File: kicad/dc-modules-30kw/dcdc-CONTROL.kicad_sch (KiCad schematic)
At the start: 35 parts

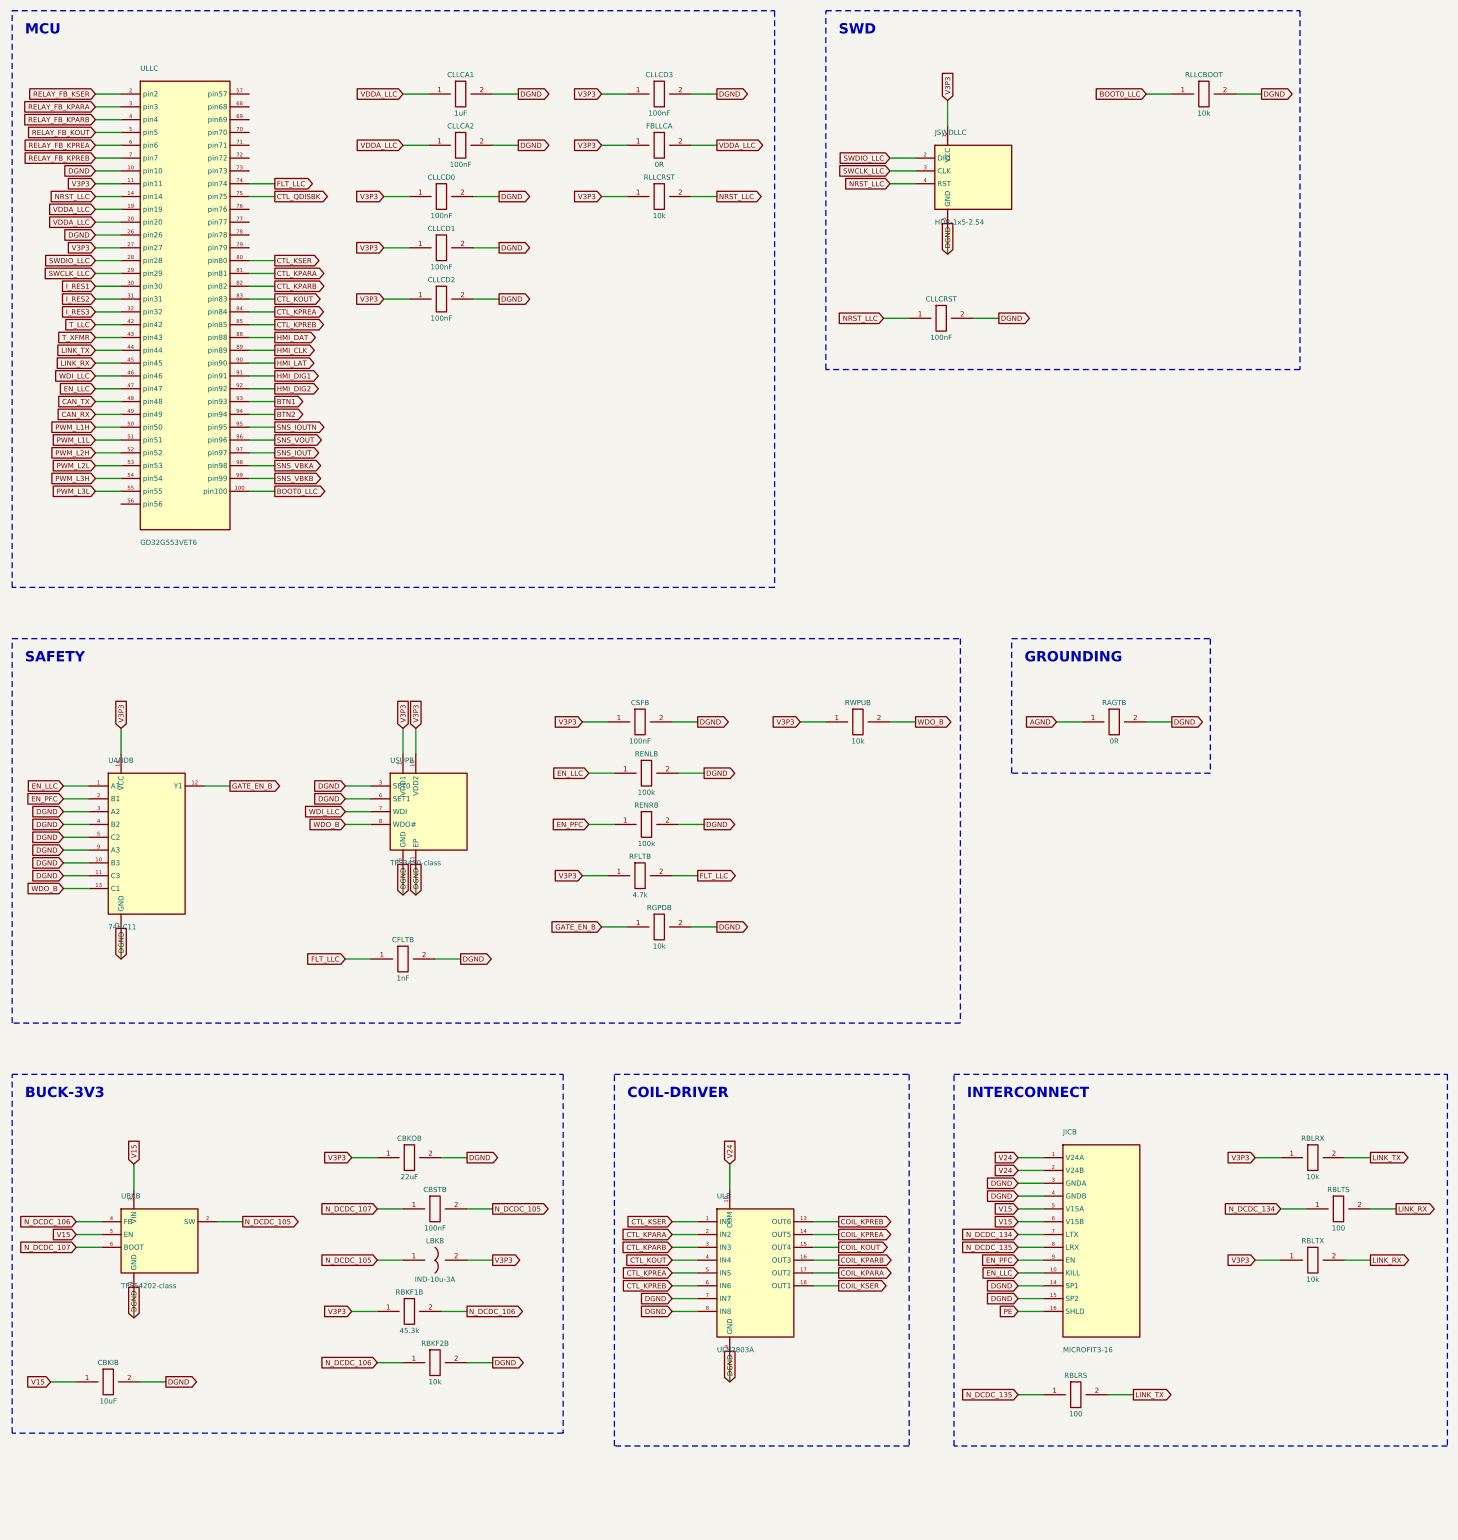
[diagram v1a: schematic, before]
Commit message: Rebuild the GD32G553VET6 pin map against the datasheet
The map was STM32G474-derived and headed pin(symbolic); gate item A6 had
recorded the GD32G553 check as pending and it was never closed. It put the
fault output on pin 74 (VSS) and BOOT0 on pin 100 (VDD) -- two hard shorts
-- and SWD on PA6/PA7, so the part was also unprogrammable as drawn.

Allocated against GD32G553xx Rev 2.0 Table 2-4 for the 120 kW worst case
(59 PFC / 80 LLC signals on 100 pins), then adversarially audited. The audit
caught a safety-critical error in the first LLC pass: PA6 cannot be
TIMER0_BRKIN0 and TIMER7_BRKIN0 at once (AF6 vs AF4, one AFSEL per pin),
which would have left four legs -- eight switches at 120 kW -- with no
hardware fault shutdown. FLT_LLC now lands on three pins, one per advanced
timer. VBAT is tied to V3P3 only; grounding it would unpower the backup
domain and kill PC13, which now carries one of those break inputs.

Applied through the remap, so the emitted netlists carry real package pins:
BOOT0 95, SWDIO 76, SWCLK 77, VDDA 37, VSSA 35, VREFP 36, all five VDD/VSS
pairs populated. Both verifiers still 100.00% (1735/1735 pins, 608
components); all review checks pass.

Four architecture decisions are documented as open rather than defaulted:
HRTIMER-vs-advanced-timer for the LLC (HRTIMER has 16 outputs, the LLC needs
24), the PFC ADC interleave scheme, LLC fan channels, and IOUT differential
mode. The map is correct and can no longer short a rail, but is not frozen.

Co-Authored-By: Claude Fable 5 <noreply@anthropic.com>
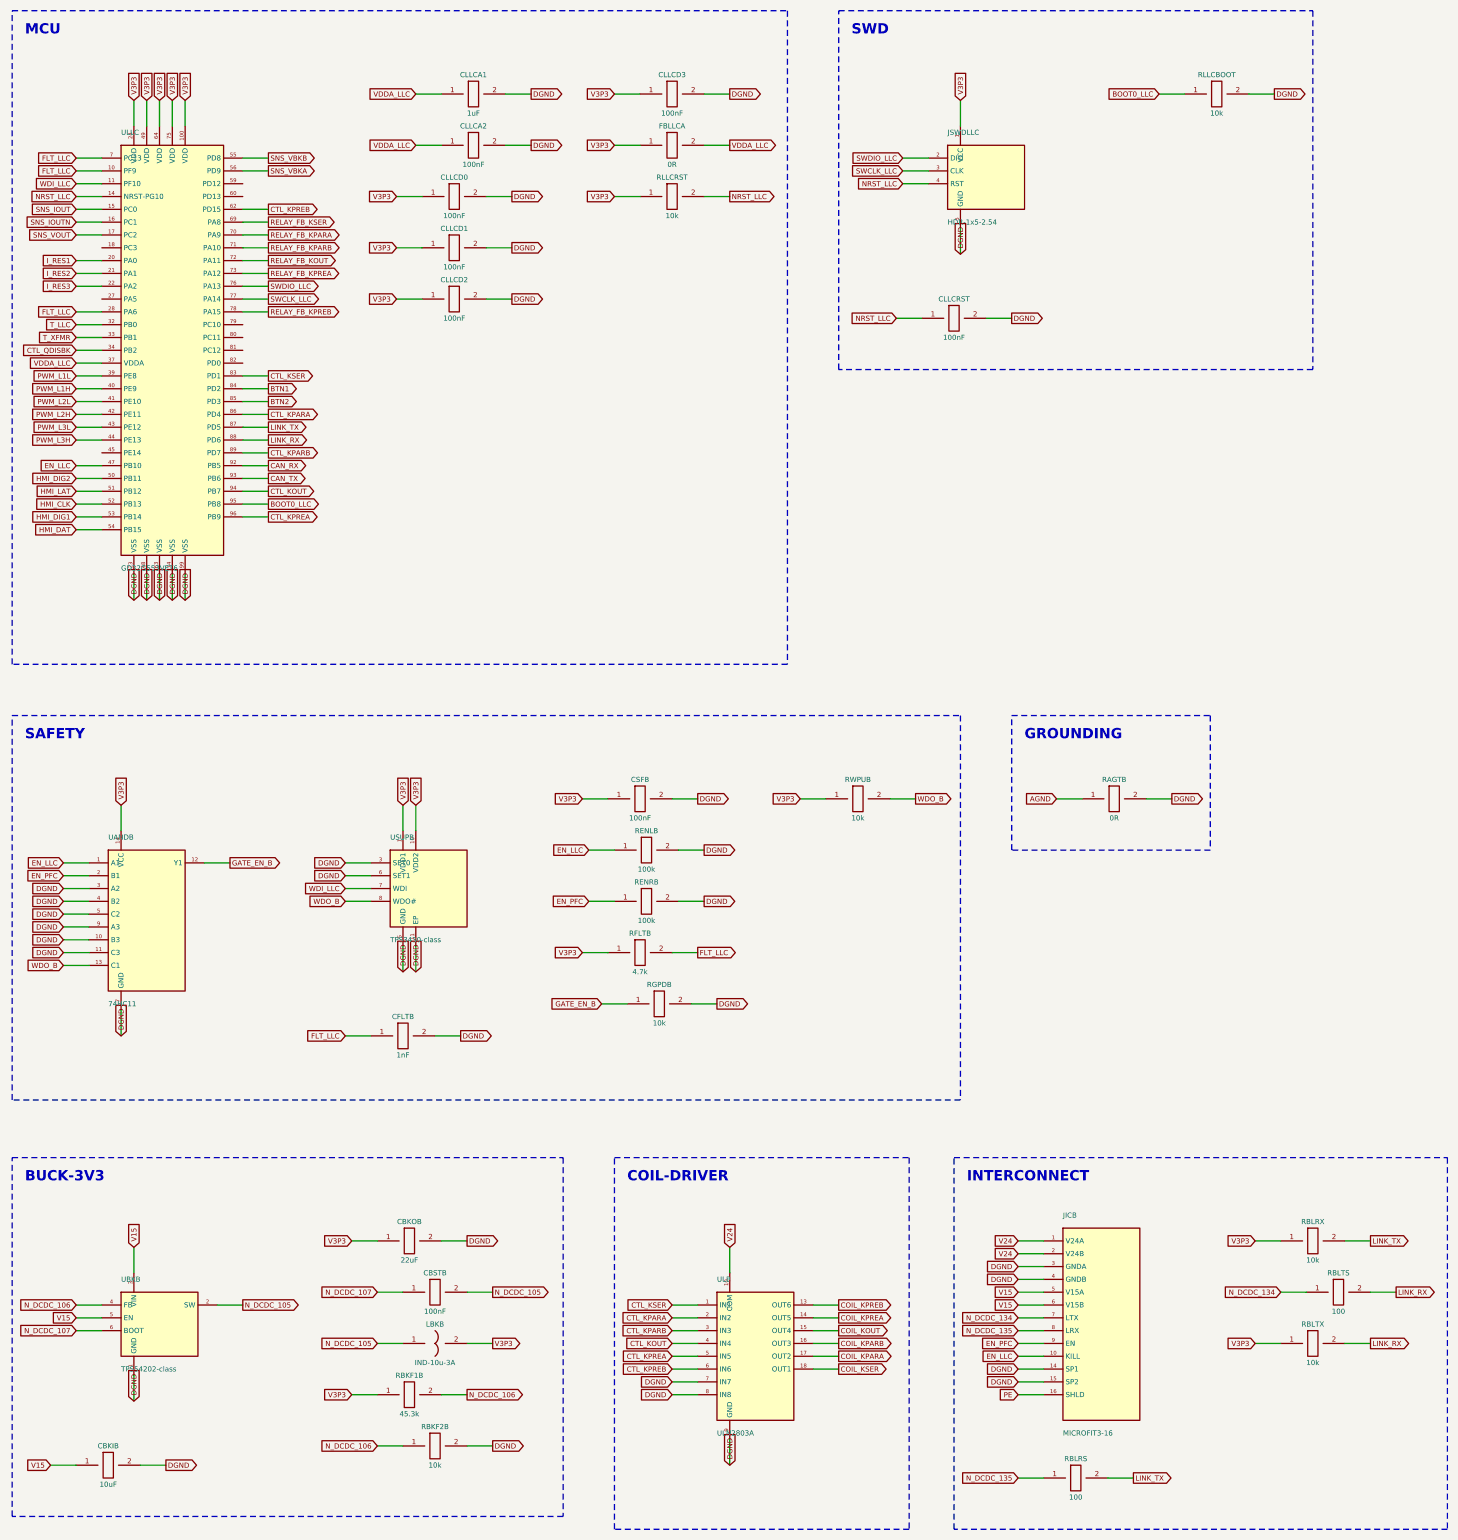
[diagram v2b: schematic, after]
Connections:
- net BOOT0_LLC: now also ULLC.95 (PB8); no longer ULLC.100 (pin100)
- net BTN1: now also ULLC.84 (PD2); no longer ULLC.93 (pin93)
- net BTN2: now also ULLC.85 (PD3); no longer ULLC.94 (pin94)
- net CAN_RX: now also ULLC.92 (PB5); no longer ULLC.49 (pin49)
- net CAN_TX: now also ULLC.93 (PB6); no longer ULLC.48 (pin48)
- net CTL_KOUT: now also ULLC.94 (PB7); no longer ULLC.83 (pin83)
- net CTL_KPARA: now also ULLC.86 (PD4); no longer ULLC.81 (pin81)
- net CTL_KPARB: now also ULLC.89 (PD7); no longer ULLC.82 (pin82)
- net CTL_KPREA: now also ULLC.96 (PB9); no longer ULLC.84 (pin84)
- net CTL_KPREB: now also ULLC.62 (PD15); no longer ULLC.85 (pin85)
- net CTL_KSER: now also ULLC.83 (PD1); no longer ULLC.80 (pin80)
- net CTL_QDISBK: now also ULLC.34 (PB2); no longer ULLC.75 (pin75)
- net DGND: now also ULLC.23 (VSS), ULLC.48 (VSS), ULLC.63 (VSS), ULLC.74 (VSS), ULLC.99 (VSS); no longer ULLC.10 (pin10), ULLC.26 (pin26)
- net FLT_LLC: now also ULLC.10 (PF9), ULLC.28 (PA6), ULLC.7 (PC13); no longer ULLC.74 (pin74)
- net HMI_CLK: now also ULLC.52 (PB13); no longer ULLC.89 (pin89)
- net HMI_DAT: now also ULLC.54 (PB15); no longer ULLC.88 (pin88)
- net HMI_DIG1: now also ULLC.53 (PB14); no longer ULLC.91 (pin91)
- net HMI_DIG2: now also ULLC.50 (PB11); no longer ULLC.92 (pin92)
- net HMI_LAT: now also ULLC.51 (PB12); no longer ULLC.90 (pin90)
- net I_RES1: now also ULLC.20 (PA0); no longer ULLC.30 (pin30)
- net I_RES2: now also ULLC.21 (PA1); no longer ULLC.31 (pin31)
- net I_RES3: now also ULLC.22 (PA2); no longer ULLC.32 (pin32)
- net LINK_RX: now also ULLC.88 (PD6); no longer ULLC.45 (pin45)
- net LINK_TX: now also ULLC.87 (PD5); no longer ULLC.44 (pin44)
- net PWM_L1H: now also ULLC.40 (PE9); no longer ULLC.50 (pin50)
- net PWM_L1L: now also ULLC.39 (PE8); no longer ULLC.51 (pin51)
- net PWM_L2H: now also ULLC.42 (PE11); no longer ULLC.52 (pin52)
- net PWM_L2L: now also ULLC.41 (PE10); no longer ULLC.53 (pin53)
- net PWM_L3H: now also ULLC.44 (PE13); no longer ULLC.54 (pin54)
- net PWM_L3L: now also ULLC.43 (PE12); no longer ULLC.55 (pin55)
- net RELAY_FB_KOUT: now also ULLC.72 (PA11); no longer ULLC.5 (pin5)
- net RELAY_FB_KPARA: now also ULLC.70 (PA9); no longer ULLC.3 (pin3)
- net RELAY_FB_KPARB: now also ULLC.71 (PA10); no longer ULLC.4 (pin4)
- net RELAY_FB_KPREA: now also ULLC.73 (PA12); no longer ULLC.6 (pin6)
- net RELAY_FB_KPREB: now also ULLC.78 (PA15); no longer ULLC.7 (pin7)
- net RELAY_FB_KSER: now also ULLC.69 (PA8); no longer ULLC.2 (pin2)
- net SNS_IOUT: now also ULLC.15 (PC0); no longer ULLC.97 (pin97)
- net SNS_IOUTN: now also ULLC.16 (PC1); no longer ULLC.95 (pin95)
- net SNS_VBKA: now also ULLC.56 (PD9); no longer ULLC.98 (pin98)
- net SNS_VBKB: now also ULLC.55 (PD8); no longer ULLC.99 (pin99)
- net SNS_VOUT: now also ULLC.17 (PC2); no longer ULLC.96 (pin96)
- net SWCLK_LLC: now also ULLC.77 (PA14); no longer ULLC.29 (pin29)
- net SWDIO_LLC: now also ULLC.76 (PA13); no longer ULLC.28 (pin28)
- net T_LLC: now also ULLC.32 (PB0); no longer ULLC.42 (pin42)
- net T_XFMR: now also ULLC.33 (PB1); no longer ULLC.43 (pin43)
- net V3P3: now also ULLC.100 (VDD), ULLC.24 (VDD), ULLC.49 (VDD), ULLC.64 (VDD), ULLC.75 (VDD); no longer ULLC.11 (pin11), ULLC.27 (pin27)
- net VDDA_LLC: now also ULLC.37 (VDDA); no longer ULLC.19 (pin19), ULLC.20 (pin20)
- net WDI_LLC: now also ULLC.11 (PF10); no longer ULLC.46 (pin46)
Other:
- moved on the sheet: CBKIB, CBKOB, CBSTB, CFLTB, CLLCA1, CLLCA2, CLLCD0, CLLCD1, CLLCD2, CLLCD3, CLLCRST, CSFB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
